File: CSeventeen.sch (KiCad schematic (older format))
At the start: 1 part, among them U2 MOS_8501

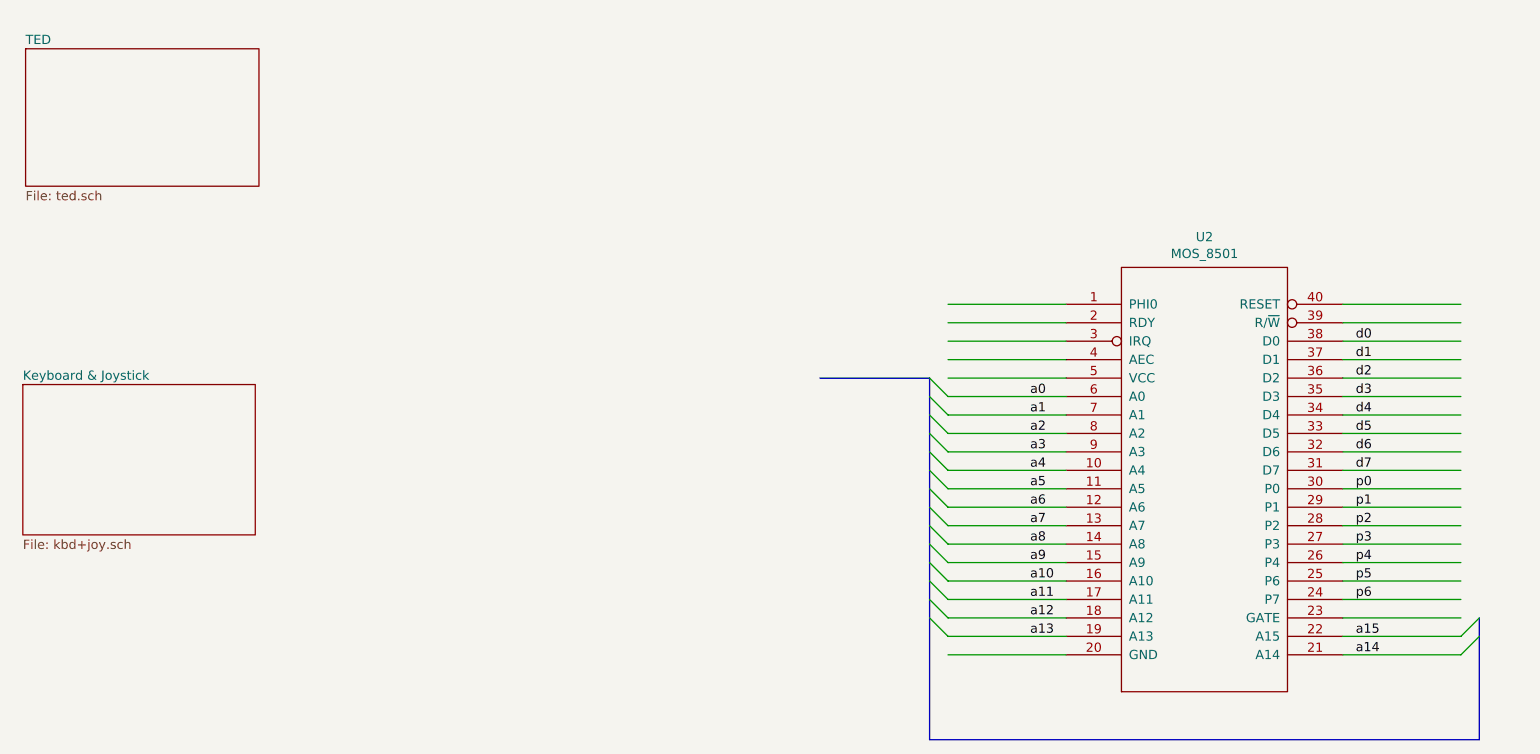
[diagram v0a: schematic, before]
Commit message: Add RAM and Expansion Port
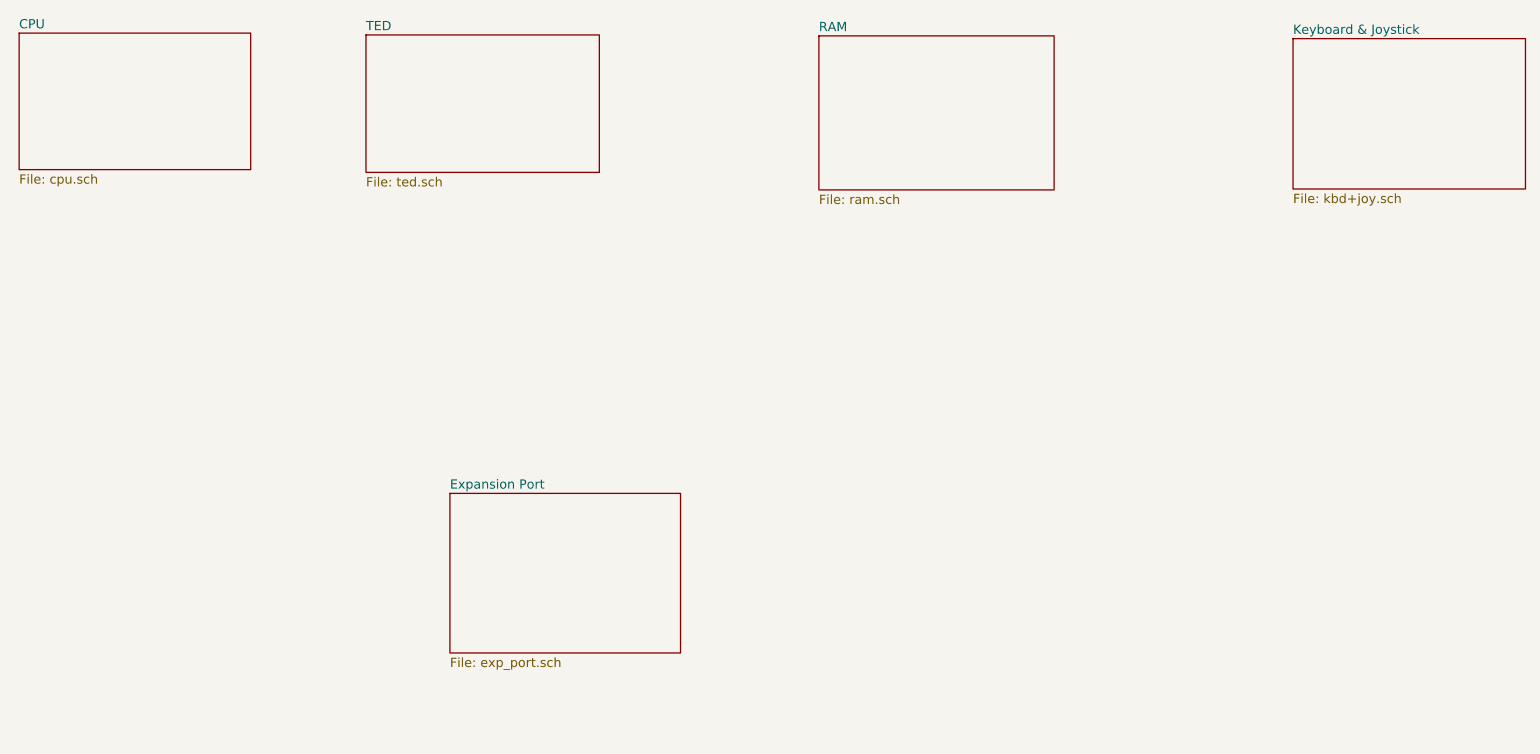
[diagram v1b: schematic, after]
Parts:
- removed U2: MOS_8501, MODULE, symbol MOS_8501:MOS_8501
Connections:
- net labels removed: a0, a1, a10, a11, a12, a13, a14, a15, a2, a3, a4, a5, a6, a7, a8, a9, d0, d1, d2, d3, d4, d5, d6, d7, p0, p1, p2, p3, p4, p5, p6
- wire segments 40 -> 0
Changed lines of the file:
@@
 $Descr A4 11693 8268
 encoding utf-8
-Sheet 1 3
+Sheet 1 6
 Title ""
 Date ""
@@
 Comment4 ""
 $EndDescr
-$Comp
-L MOS_8501:MOS_8501 U2
-U 1 1 5DDE292A
-P 7865 3650
-F 0 "U2" H 7865 4965 50  0000 C CNN
-F 1 "MOS_8501" H 7865 4874 50  0000 C CNN
-F 2 "MODULE" H 7865 3650 50  0001 C CNN
-F 3 "DOCUMENTATION" H 7865 3650 50  0001 C CNN
-	1    7865 3650
-	1    0    0    -1
-$EndComp
-Wire Wire Line
-	7115 2700 6475 2700
-Wire Wire Line
-	7115 2800 6475 2800
-Wire Wire Line
-	7115 2900 6475 2900
-Wire Wire Line
-	7115 3000 6475 3000
-Wire Wire Line
-	7115 3100 6475 3100
-Wire Wire Line
-	7115 3200 6475 3200
-Wire Wire Line
-	7115 3300 6475 3300
-Wire Wire Line
-	7115 3400 6475 3400
-Wire Wire Line
-	7115 3500 6475 3500
-Wire Wire Line
-	7115 3600 6475 3600
-Wire Wire Line
-	7115 3700 6475 3700
-Wire Wire Line
-	7115 3800 6475 3800
-Wire Wire Line
-	7115 3900 6475 3900
-Wire Wire Line
-	7115 4000 6475 4000
-Wire Wire Line
-	7115 4100 6475 4100
-Wire Wire Line
-	7115 4200 6475 4200
-Wire Wire Line
-	7115 4300 6475 4300
-Wire Wire Line
-	7115 4400 6475 4400
-Wire Wire Line
-	7115 4500 6475 4500
-Wire Wire Line
-	7115 4600 6475 4600
-Wire Wire Line
-	9255 2700 8615 2700
-Wire Wire Line
-	9255 2800 8615 2800
-Wire Wire Line
-	9255 2900 8615 2900
-Wire Wire Line
-	9255 3000 8615 3000
-Wire Wire Line
-	9255 3100 8615 3100
-Wire Wire Line
-	9255 3200 8615 3200
-Wire Wire Line
-	9255 3300 8615 3300
-Wire Wire Line
-	9255 3400 8615 3400
-Wire Wire Line
-	9255 3500 8615 3500
-Wire Wire Line
-	9255 3600 8615 3600
-Wire Wire Line
-	9255 3700 8615 3700
-Wire Wire Line
-	9255 3800 8615 3800
-Wire Wire Line
-	9255 3900 8615 3900
-Wire Wire Line
-	9255 4000 8615 4000
-Wire Wire Line
-	9255 4100 8615 4100
-Wire Wire Line
-	9255 4200 8615 4200
-Wire Wire Line
-	9255 4300 8615 4300
-Wire Wire Line
-	9255 4400 8615 4400
-Wire Wire Line
-	9255 4500 8615 4500
-Wire Wire Line
-	9255 4600 8615 4600
-Entry Wire Line
-	6375 3100 6475 3200
-Entry Wire Line
-	6375 3200 6475 3300
-Entry Wire Line
-	6375 3300 6475 3400
-Entry Wire Line
-	6375 3400 6475 3500
-Entry Wire Line
-	6375 3500 6475 3600
-Entry Wire Line
-	6375 3600 6475 3700
-Entry Wire Line
-	6375 3700 6475 3800
-Entry Wire Line
-	6375 3800 6475 3900
-Entry Wire Line
-	6375 3900 6475 4000
-Entry Wire Line
-	6375 4000 6475 4100
-Entry Wire Line
-	6375 4100 6475 4200
-Entry Wire Line
-	6375 4200 6475 4300
-Entry Wire Line
-	6375 4300 6475 4400
-Entry Wire Line
-	6375 4400 6475 4500
-Entry Wire Line
-	9355 4400 9255 4500
-Entry Wire Line
-	9255 4600 9355 4500
-Wire Bus Line
-	9355 5060 6375 5060
-Wire Bus Line
-	6375 3100 5780 3100
-Text Label 8685 4500 0    50   ~ 0
-a15
-Text Label 8685 4600 0    50   ~ 0
-a14
-Text Label 8685 2900 0    50   ~ 0
-d0
-Text Label 8685 3000 0    50   ~ 0
-d1
-Text Label 8685 3100 0    50   ~ 0
-d2
-Text Label 8685 3200 0    50   ~ 0
-d3
-Text Label 8685 3300 0    50   ~ 0
-d4
-Text Label 8685 3400 0    50   ~ 0
-d5
-Text Label 8685 3500 0    50   ~ 0
-d6
-Text Label 8685 3600 0    50   ~ 0
-d7
-Text Label 8685 3700 0    50   ~ 0
-p0
-Text Label 8685 3800 0    50   ~ 0
-p1
-Text Label 8685 3900 0    50   ~ 0
-p2
-Text Label 8685 4000 0    50   ~ 0
-p3
-Text Label 8685 4100 0    50   ~ 0
-p4
-Text Label 8685 4200 0    50   ~ 0
-p5
-Text Label 8685 4300 0    50   ~ 0
-p6
-Text Label 6920 3200 0    50   ~ 0
-a0
-Text Label 6920 3300 0    50   ~ 0
-a1
-Text Label 6920 3400 0    50   ~ 0
-a2
-Text Label 6920 3500 0    50   ~ 0
-a3
-Text Label 6920 3600 0    50   ~ 0
-a4
-Text Label 6920 3700 0    50   ~ 0
-a5
-Text Label 6920 3800 0    50   ~ 0
-a6
-Text Label 6920 3900 0    50   ~ 0
-a7
-Text Label 6920 4000 0    50   ~ 0
-a8
-Text Label 6920 4100 0    50   ~ 0
-a9
-Text Label 6920 4200 0    50   ~ 0
-a10
-Text Label 6920 4300 0    50   ~ 0
-a11
-Text Label 6920 4400 0    50   ~ 0
-a12
-Text Label 6920 4500 0    50   ~ 0
-a13
 $Sheet
-S 1475 1315 1265 745
+S 3320 1240 1265 745
 U 5DE044CB
 F0 "TED" 50
 F1 "ted.sch" 50
 $EndSheet
-Wire Bus Line
-	9355 4400 9355 5060
-Wire Bus Line
-	6375 3100 6375 5060
 $Sheet
-S 1460 3135 1260 815
+S 8345 1260 1260 815
 U 5DECEF6F
 F0 "Keyboard & Joystick" 50
 F1 "kbd+joy.sch" 50
 $EndSheet
+$Sheet
+S 5775 1245 1275 835
+U 5E4A465A
+F0 "RAM" 50
+F1 "ram.sch" 50
+$EndSheet
+$Sheet
+S 1440 1230 1255 740
+U 5E4A81E1
+F0 "CPU" 50
+F1 "cpu.sch" 50
+$EndSheet
+$Sheet
+S 3775 3725 1250 865
+U 5E6A379E
+F0 "Expansion Port" 50
+F1 "exp_port.sch" 50
+$EndSheet
 $EndSCHEMATC

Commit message: Forgotten libs...
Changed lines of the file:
@@
 $Descr A4 11693 8268
 encoding utf-8
-Sheet 1 6
+Sheet 1 7
 Title ""
 Date ""
@@
 F1 "exp_port.sch" 50
 $EndSheet
+$Sheet
+S 6055 3695 1375 870
+U 5EACE220
+F0 "Misc" 50
+F1 "misc.sch" 50
+$EndSheet
 $EndSCHEMATC

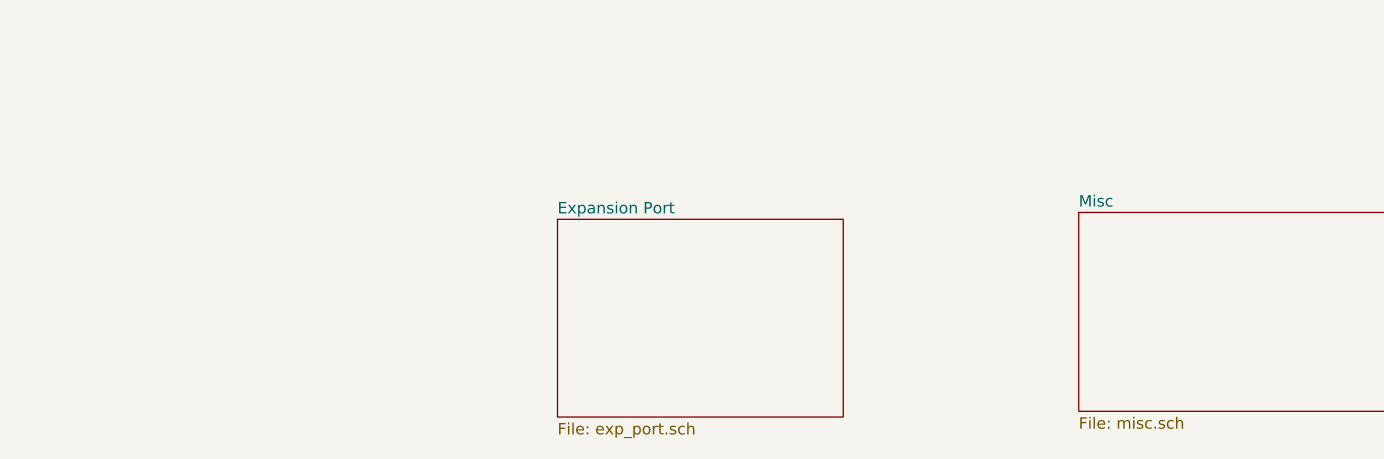
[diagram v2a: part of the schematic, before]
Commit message: Add Datassette and power
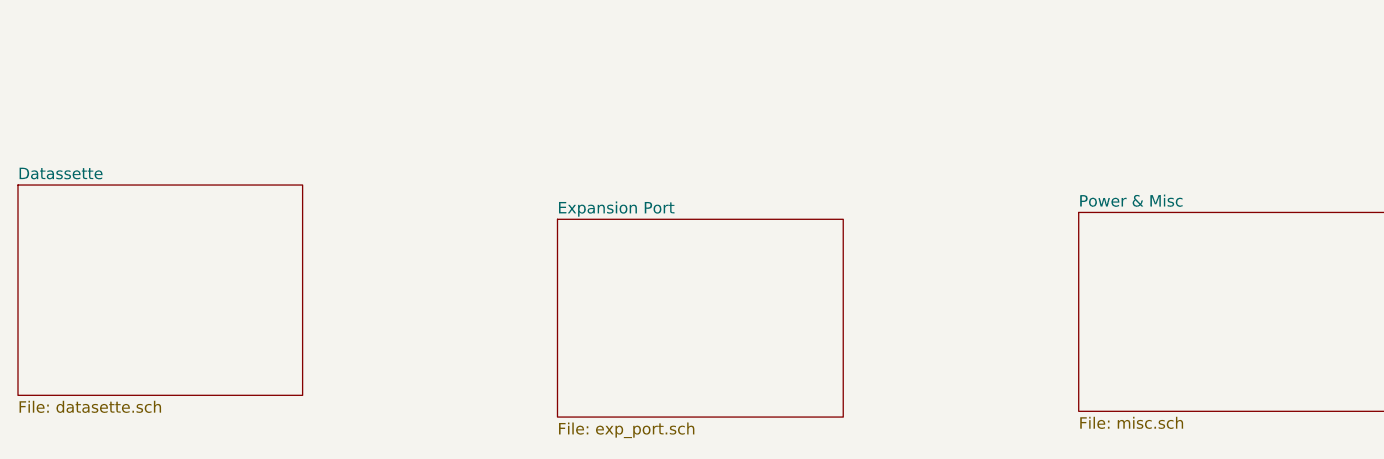
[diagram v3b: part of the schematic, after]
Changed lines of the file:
@@
 $Descr A4 11693 8268
 encoding utf-8
-Sheet 1 7
+Sheet 1 8
 Title ""
 Date ""
@@
 S 6055 3695 1375 870
 U 5EACE220
-F0 "Misc" 50
+F0 "Power & Misc" 50
 F1 "misc.sch" 50
 $EndSheet
+$Sheet
+S 1415 3575 1245 920
+U 5ECB474B
+F0 "Datassette" 50
+F1 "datasette.sch" 50
+$EndSheet
 $EndSCHEMATC

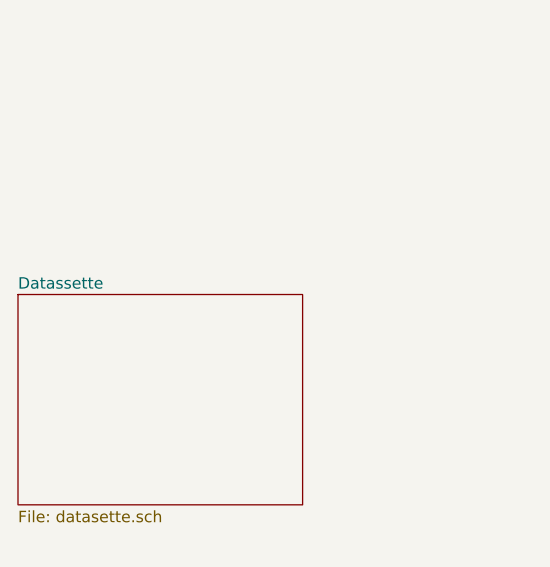
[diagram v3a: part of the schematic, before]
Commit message: Add Serial Bus
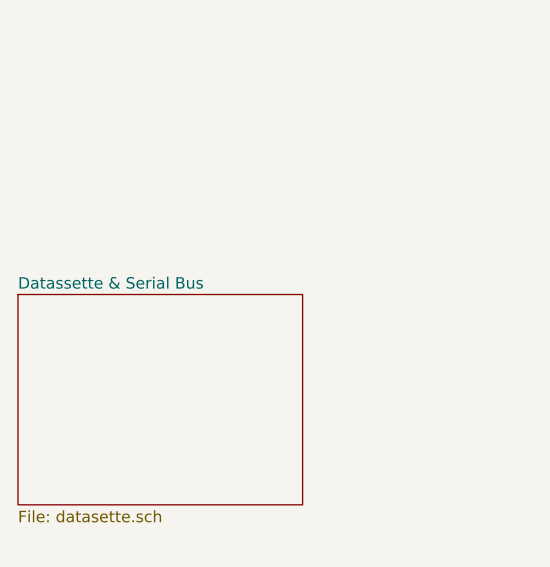
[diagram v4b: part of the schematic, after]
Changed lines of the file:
@@
 S 1415 3575 1245 920
 U 5ECB474B
-F0 "Datassette" 50
+F0 "Datassette & Serial Bus" 50
 F1 "datasette.sch" 50
 $EndSheet
